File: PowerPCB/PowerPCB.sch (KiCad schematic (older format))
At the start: 38 parts, among them J1 Conn_01x03_Male, J2 Conn_01x10_Male, J5 Conn_01x07_Male, K1 1721081-5, K2 1721081-5, U1 NCP1117-3.3_SOT223, U2 STM32F413ZHTx, U3 NCP1117-5.0_SOT223, U4 MCP2562-E-P, U5 MCP2562-E-P

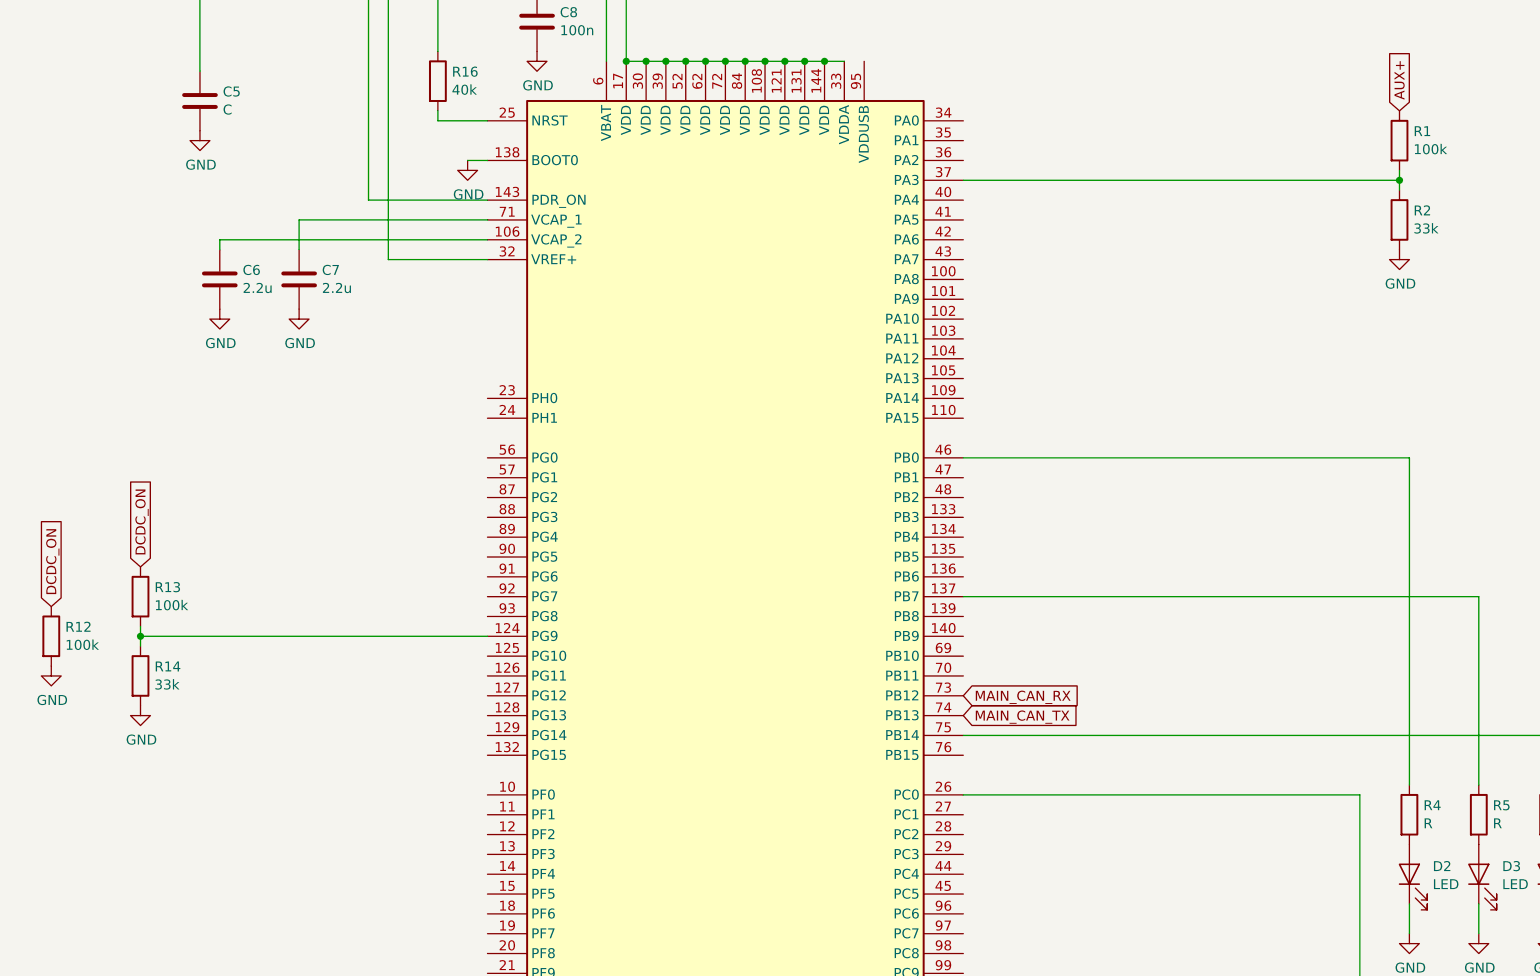
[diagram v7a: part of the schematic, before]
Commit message: Added input protection circuitry as sub-schematic
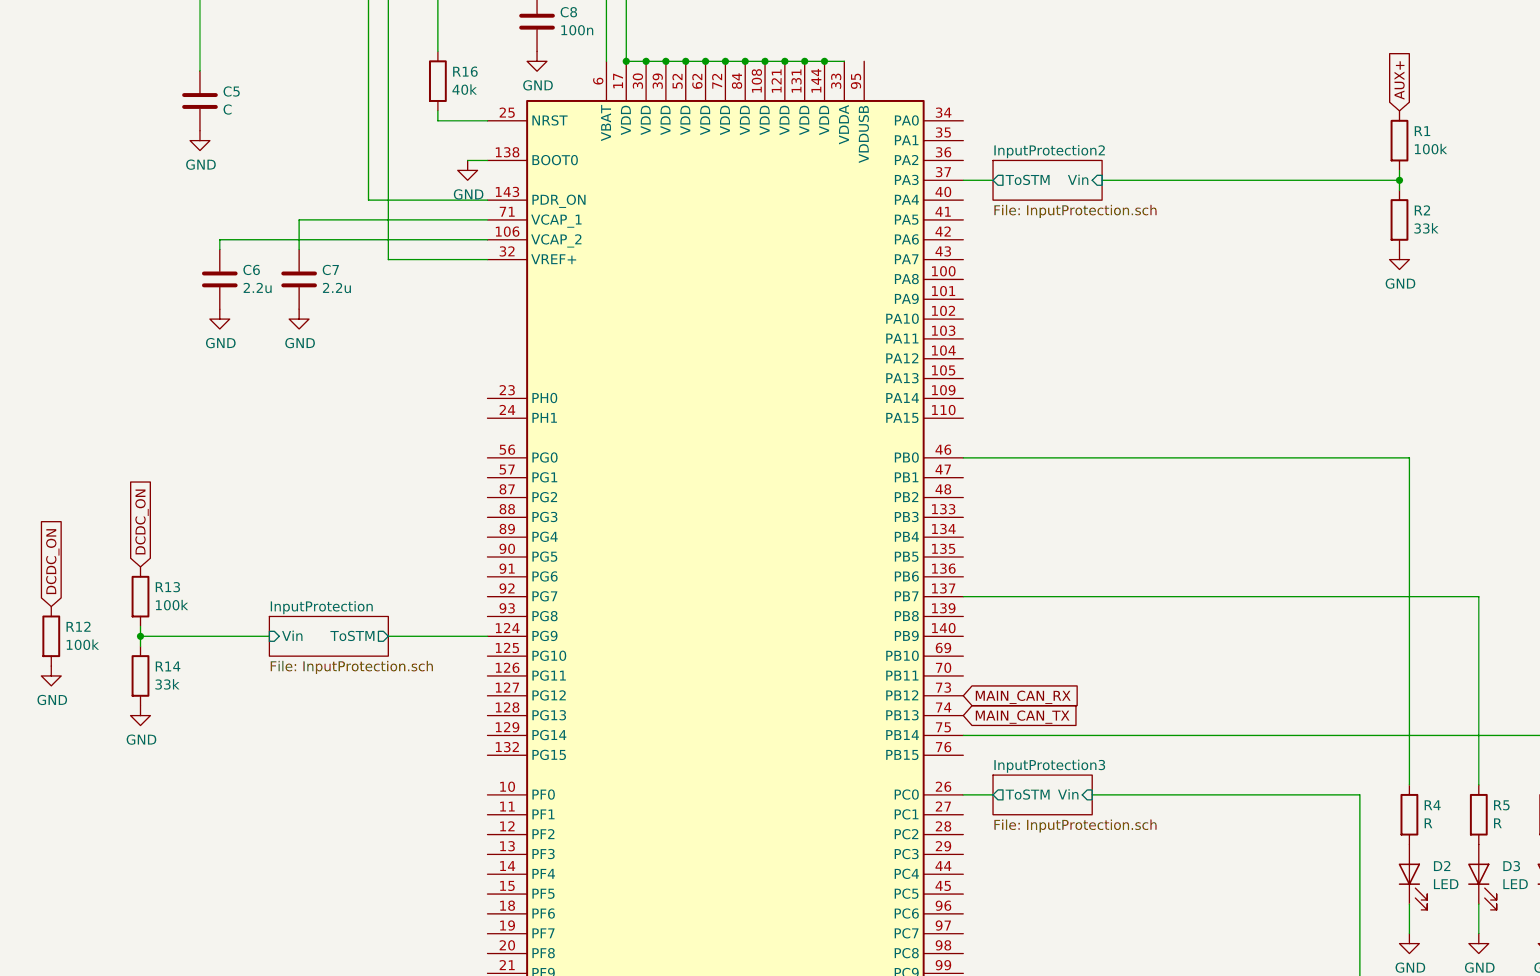
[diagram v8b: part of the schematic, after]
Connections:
- net InputProtection2/Vin: now reaches R1.2, R2.1
- net InputProtection2/Vin: no longer U2.37 (PA3)
- net InputProtection/Vin: now reaches R13.2, R14.1
- net InputProtection/Vin: no longer U2.124 (PG9)
- net InputProtection3/Vin: now reaches R10.2, R11.1
- net InputProtection3/Vin: no longer U2.26 (PC0)
- new net InputProtection/ToSTM: U2.124 (PG9)
- new net InputProtection2/ToSTM: U2.37 (PA3)
- new net InputProtection3/ToSTM: U2.26 (PC0)
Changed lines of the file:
@@
 $Descr A3 16535 11693
 encoding utf-8
-Sheet 1 2
+Sheet 1 5
 Title ""
 Date ""
@@
 DCDC+
 Wire Wire Line
-	14000 2550 11800 2550
+	14000 2550 12500 2550
 Connection ~ 14000 2550
 Wire Wire Line
@@
 Wire Wire Line
 	13800 7300 13800 5650
-Wire Wire Line
-	13800 5650 11800 5650
 Connection ~ 14050 7300
 Wire Wire Line
@@
 	7650 4800 7650 4850
 Wire Wire Line
-	9400 4850 7650 4850
+	9400 4850 8900 4850
 Connection ~ 7650 4850
 Wire Wire Line
@@
 Wire Wire Line
 	9650 1550 10000 1550
+Wire Wire Line
+	8300 4850 7650 4850
+$Sheet
+S 8300 4750 600  200
+U 5EE2B52D
+F0 "InputProtection" 50
+F1 "InputProtection.sch" 50
+F2 "Vin" I L 8300 4850 50
+F3 "ToSTM" O R 8900 4850 50
+$EndSheet
+$Sheet
+S 11950 2450 550  200
+U 5EE3728E
+F0 "InputProtection2" 50
+F1 "InputProtection.sch" 50
+F2 "Vin" I R 12500 2550 50
+F3 "ToSTM" O L 11950 2550 50
+$EndSheet
+Wire Wire Line
+	11950 2550 11800 2550
+$Sheet
+S 11950 5550 500  200
+U 5EE40591
+F0 "InputProtection3" 50
+F1 "InputProtection.sch" 50
+F2 "Vin" I R 12450 5650 50
+F3 "ToSTM" O L 11950 5650 50
+$EndSheet
+Wire Wire Line
+	11800 5650 11950 5650
+Wire Wire Line
+	12450 5650 13800 5650
 $EndSCHEMATC
